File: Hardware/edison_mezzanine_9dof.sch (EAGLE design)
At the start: 43 parts, among them U1 LSM9DS0, U2 EDISON_CONNECTOR_FULLMOUNTING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, U3 EDISON_CONNECTOR_FULLHEADER

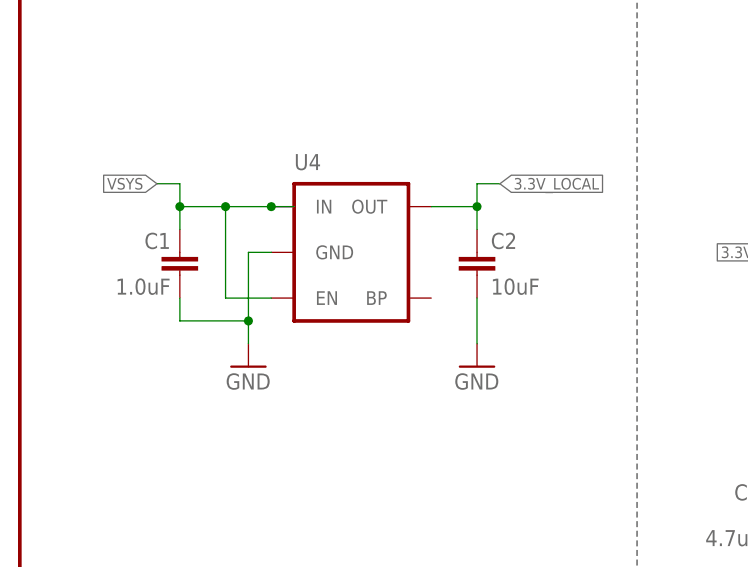
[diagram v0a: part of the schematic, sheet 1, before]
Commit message: Fixed hanging wire from LDO and added LDO chip name to schematic.
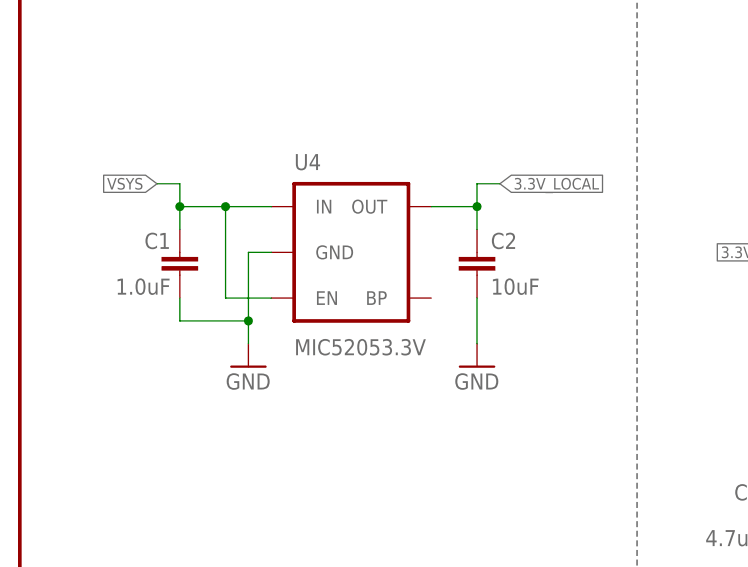
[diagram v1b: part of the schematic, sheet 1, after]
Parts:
- U4: value (none) -> MIC52053.3V
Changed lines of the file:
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@@
 <setting verticaltext="up"/>
 </settings>
-<grid distance="0.1" unitdist="inch" unit="inch" style="lines" multiple="1" display="yes" altdistance="0.01" altunitdist="inch" altunit="inch"/>
+<grid distance="0.1" unitdist="inch" unit="inch" style="lines" multiple="1" display="no" altdistance="0.01" altunitdist="inch" altunit="inch"/>
 <layers>
 <layer number="1" name="Top" color="4" fill="1" visible="no" active="no"/>
@@
 <part name="SJ2" library="SparkFun-Passives" deviceset="JUMPER-PAD-3-NC_BY_PASTE" device=""/>
 <part name="SJ1" library="SparkFun-Passives" deviceset="JUMPER-PAD-3-NC_BY_PASTE" device=""/>
-<part name="U4" library="SparkFun-PowerIC" deviceset="MIC5205" device="3.3V"/>
+<part name="U4" library="SparkFun-PowerIC" deviceset="MIC5205" device="3.3V" value="MIC52053.3V"/>
 <part name="C1" library="SparkFun-Capacitors" deviceset="1.0UF-16V-10%(0603)" device="" value="1.0uF"/>
 <part name="C4" library="SparkFun-Capacitors" deviceset="0.1UF-25V(+80/-20%)(0603)" device="" value="0.1uF"/>
@@
 <wire x1="27.94" y1="129.54" x2="22.86" y2="129.54" width="0.1524" layer="91"/>
 <wire x1="22.86" y1="129.54" x2="22.86" y2="139.7" width="0.1524" layer="91"/>
-<wire x1="30.48" y1="139.7" x2="27.94" y2="139.7" width="0.1524" layer="91"/>
-<wire x1="27.94" y1="139.7" x2="22.86" y2="139.7" width="0.1524" layer="91"/>
 <wire x1="22.86" y1="139.7" x2="17.78" y2="139.7" width="0.1524" layer="91"/>
-<junction x="22.86" y="139.7"/>
 <pinref part="C1" gate="G$1" pin="1"/>
 <wire x1="17.78" y1="139.7" x2="17.78" y2="137.16" width="0.1524" layer="91"/>
@@
 <label x="15.24" y="142.24" size="1.27" layer="95" rot="R180" xref="yes"/>
 <pinref part="U4" gate="G$1" pin="IN"/>
-<junction x="27.94" y="139.7"/>
-</segment>
-</net>
+<wire x1="22.86" y1="139.7" x2="27.94" y2="139.7" width="0.1524" layer="91"/>
+<junction x="22.86" y="139.7"/>
+</segment>
+</net>

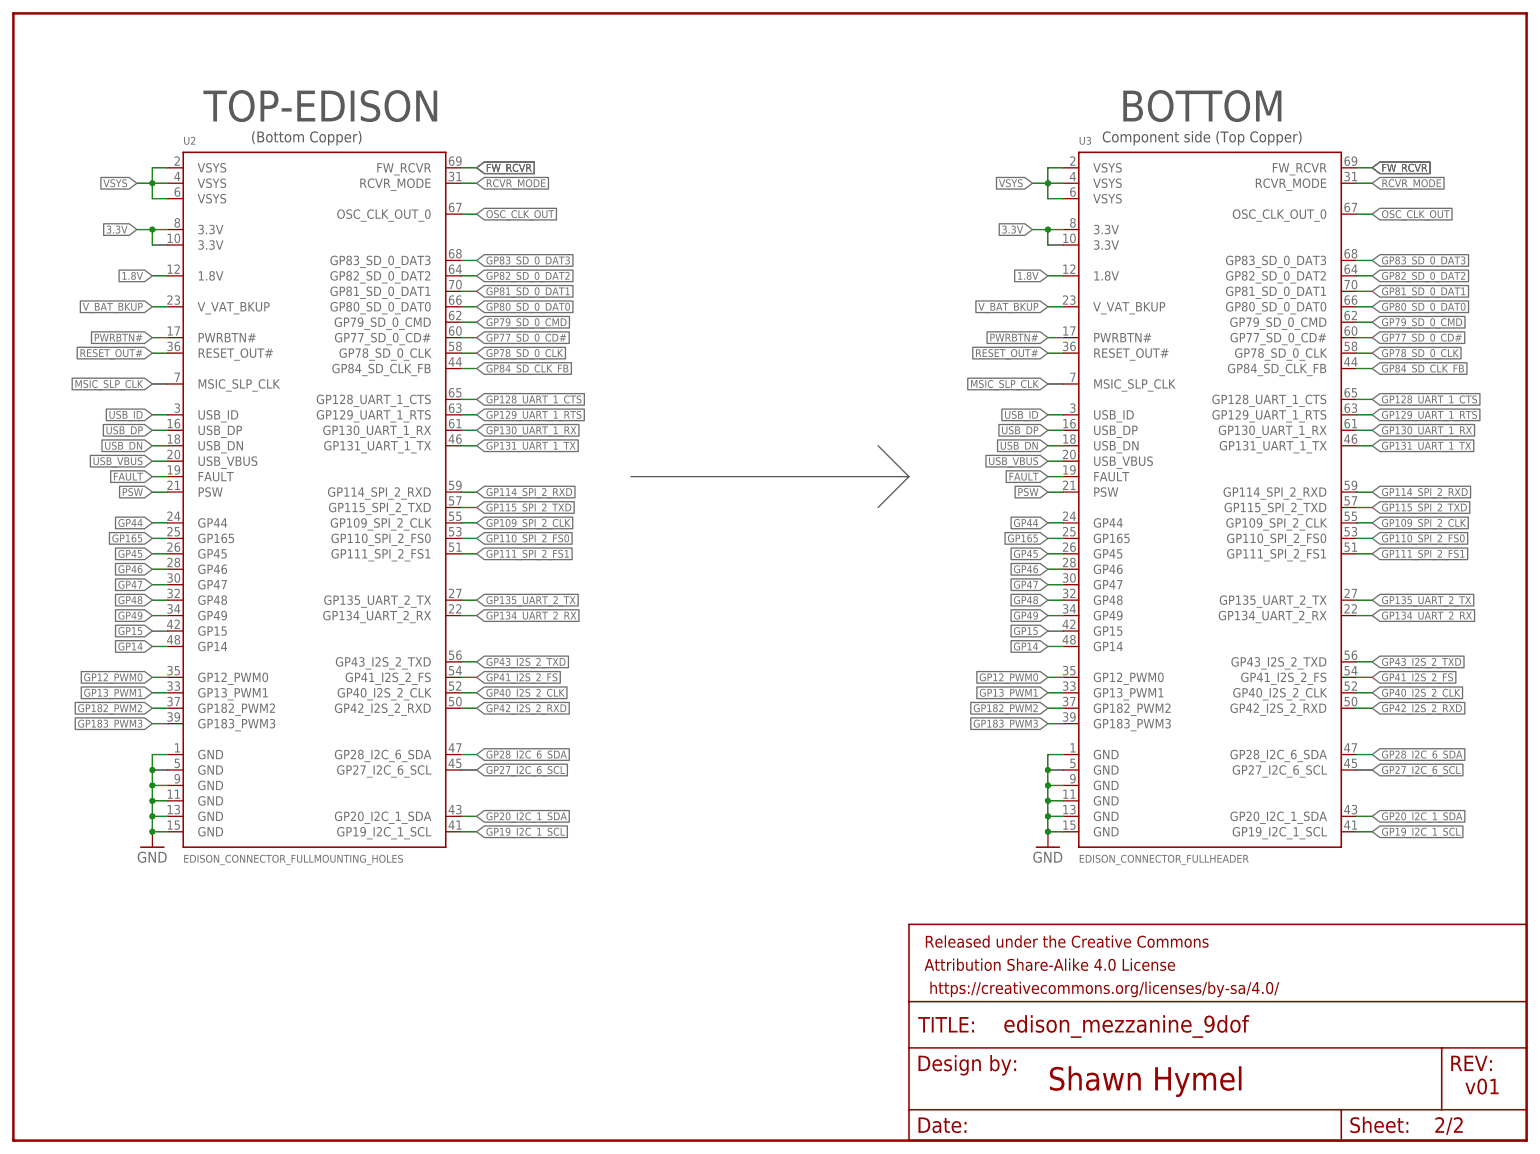
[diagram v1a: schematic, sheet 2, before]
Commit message: Added DCIN pin Corrected Header footprint Modified Name of board cleaned up units and added units cleaned up copper fills
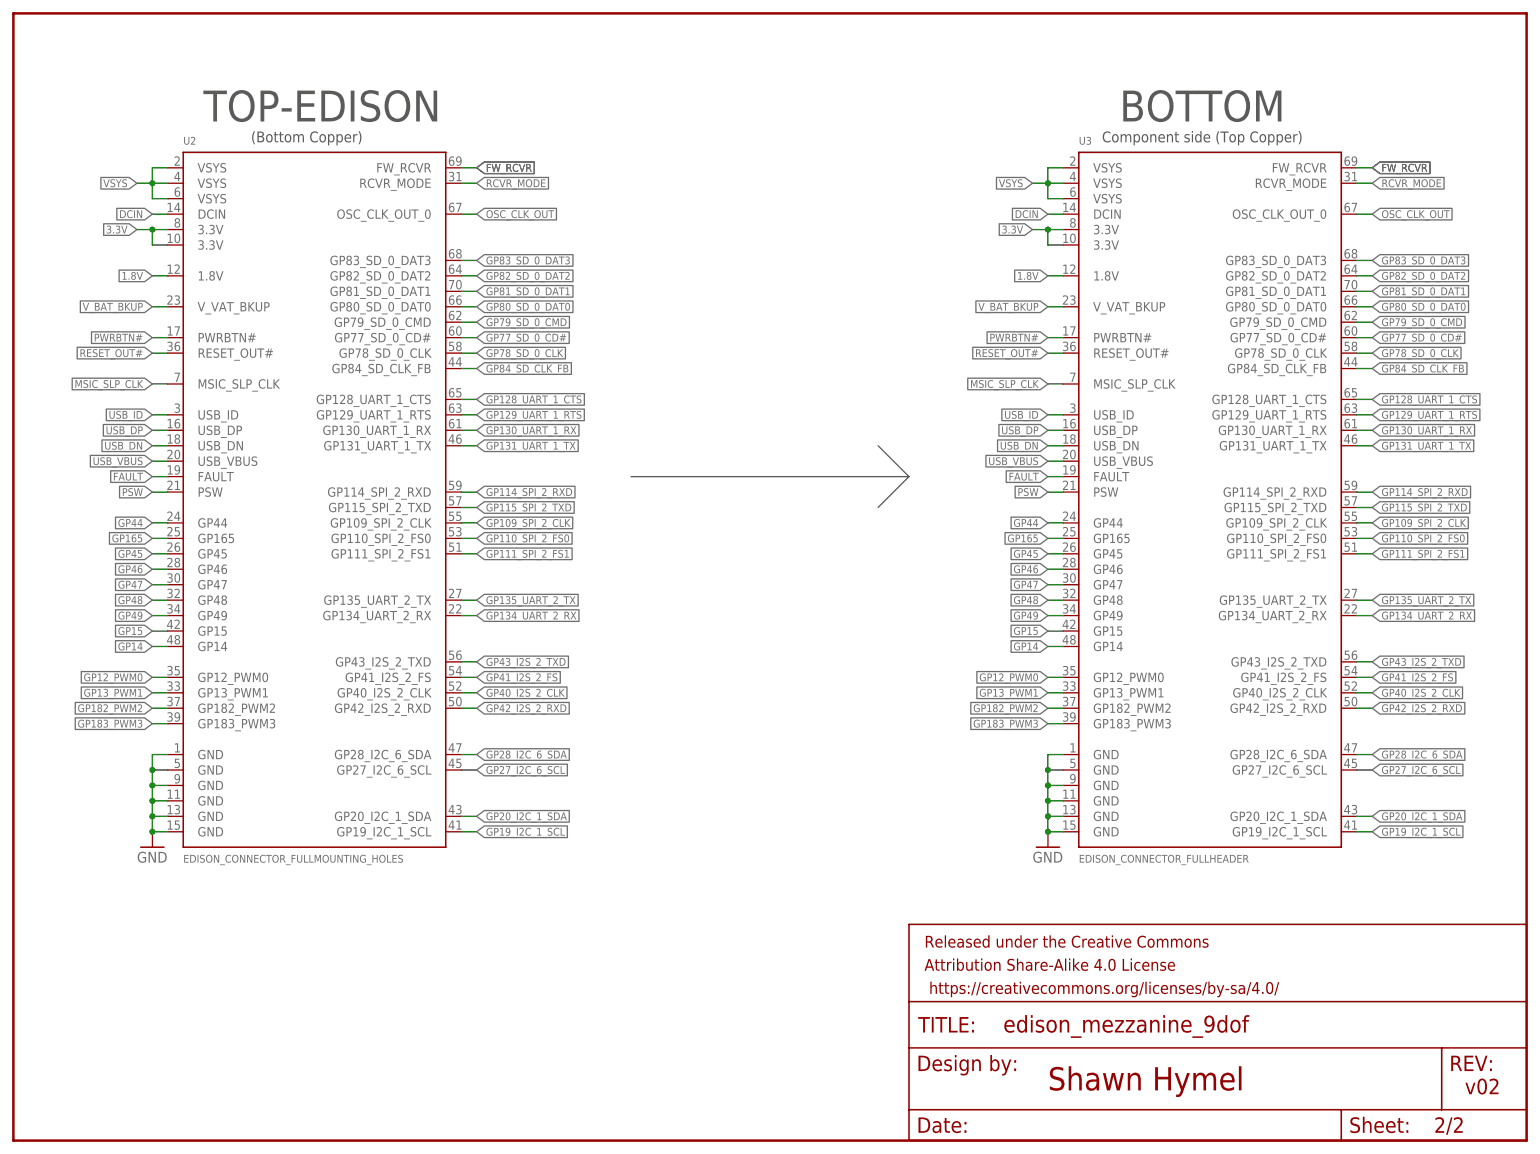
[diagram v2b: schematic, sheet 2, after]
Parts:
- removed FRAME3: FRAME-LETTER, SparkFun-Aesthetics:FRAME-LETTER
- R1, R2: value 4.7k -> DNP
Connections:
- new net DCIN: U2.DCIN, U3.DCIN
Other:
- note added: "v02"
- note removed: "v01"
- note removed: "v10"
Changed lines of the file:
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@@
 </classes>
 <parts>
-<part name="FRAME1" library="SparkFun-Aesthetics" deviceset="FRAME-LETTER" device=""/>
 <part name="LOGO2" library="SparkFun-Aesthetics" deviceset="OSHW-LOGO" device="S"/>
 <part name="LOGO3" library="SparkFun-Aesthetics" deviceset="SFE_LOGO_NAME_FLAME" device=".1_INCH"/>
@@
 <part name="C3" library="SparkFun-Capacitors" deviceset="1.0UF-16V-10%(0603)" device="" value="1.0uF"/>
 <part name="GND5" library="SparkFun-Aesthetics" deviceset="GND" device=""/>
-<part name="R1" library="SparkFun-Resistors" deviceset="10K-1%" device="RES-00824" value="4.7k"/>
-<part name="R2" library="SparkFun-Resistors" deviceset="10K-1%" device="RES-00824" value="4.7k"/>
+<part name="R1" library="SparkFun-Resistors" deviceset="10K-1%" device="RES-00824" value="DNP"/>
+<part name="R2" library="SparkFun-Resistors" deviceset="10K-1%" device="RES-00824" value="DNP"/>
 <part name="R3" library="SparkFun-Resistors" deviceset="10K-1%" device="RES-00824" value="10k"/>
 <part name="R4" library="SparkFun-Resistors" deviceset="10K-1%" device="RES-00824" value="10k"/>
@@
 <part name="FID1" library="SparkFun-Aesthetics" deviceset="FIDUCIAL" device="1X2"/>
 <part name="FID2" library="SparkFun-Aesthetics" deviceset="FIDUCIAL" device="1X2"/>
-<part name="FRAME2" library="SparkFun-Aesthetics" deviceset="FRAME-LETTER" device=""/>
-<part name="FRAME3" library="SparkFun-Aesthetics" deviceset="FRAME-LETTER" device=""/>
 <part name="SJ16" library="SparkFun-Passives" deviceset="JUMPER-PAD-2-NO" device="YES_SILK"/>
 <part name="SJ17" library="SparkFun-Passives" deviceset="JUMPER-PAD-2-NO" device="YES_SILK"/>
 <part name="FID3" library="SparkFun-Aesthetics" deviceset="FIDUCIAL" device="1X2"/>
 <part name="FID4" library="SparkFun-Aesthetics" deviceset="FIDUCIAL" device="1X2"/>
+<part name="FRAME1" library="SparkFun-Aesthetics" deviceset="FRAME-LETTER" device=""/>
+<part name="FRAME2" library="SparkFun-Aesthetics" deviceset="FRAME-LETTER" device=""/>
 </parts>
 <sheets>
@@
 <text x="45.72" y="25.4" size="2.54" layer="97" align="center">1</text>
 <text x="60.96" y="25.4" size="2.54" layer="97" align="center">0x6B</text>
-<text x="238.76" y="7.62" size="2.54" layer="94">v10</text>
-<text x="167.64" y="10.16" size="2.54" layer="94">Shawn Hymel</text>
+<text x="238.76" y="7.62" size="2.54" layer="94">v02</text>
+<text x="170.18" y="7.62" size="2.54" layer="94">Shawn Hymel</text>
 </plain>
 <instances>
-<instance part="FRAME1" gate="G$1" x="0" y="0"/>
-<instance part="FRAME1" gate="G$2" x="147.32" y="0"/>
 <instance part="LOGO2" gate="G$1" x="73.66" y="12.7"/>
 <instance part="LOGO3" gate="G$1" x="88.9" y="2.54"/>
@@
 <instance part="FID3" gate="G$1" x="246.38" y="30.48"/>
 <instance part="FID4" gate="G$1" x="241.3" y="30.48"/>
+<instance part="FRAME1" gate="G$1" x="0" y="0"/>
+<instance part="FRAME1" gate="G$2" x="147.32" y="0"/>
 </instances>
 <busses>
@@
 <text x="48.26" y="165.1" size="1.778" layer="92" align="center">(Bottom Copper)</text>
 <text x="170.18" y="10.16" size="3.81" layer="94" align="center-left">Shawn Hymel</text>
-<text x="238.76" y="7.62" size="2.54" layer="94">v01</text>
+<text x="238.76" y="7.62" size="2.54" layer="94">v02</text>
 </plain>
 <instances>
@@
 <instance part="GND4" gate="1" x="170.18" y="48.26"/>
 <instance part="FRAME2" gate="G$1" x="0" y="0"/>
-<instance part="FRAME3" gate="G$2" x="147.32" y="0"/>
+<instance part="FRAME2" gate="G$2" x="147.32" y="0"/>
 </instances>
 <busses>
@@
 </segment>
 </net>
+<net name="DCIN" class="0">
+<segment>
+<pinref part="U3" gate="G$1" pin="DCIN"/>
+<wire x1="172.72" y1="152.4" x2="170.18" y2="152.4" width="0.1524" layer="91"/>
+<label x="170.18" y="152.4" size="1.27" layer="95" rot="R180" xref="yes"/>
+</segment>
+<segment>
+<pinref part="U2" gate="G$1" pin="DCIN"/>
+<wire x1="25.4" y1="152.4" x2="22.86" y2="152.4" width="0.1524" layer="91"/>
+<label x="22.86" y="152.4" size="1.27" layer="95" rot="R180" xref="yes"/>
+</segment>
+</net>

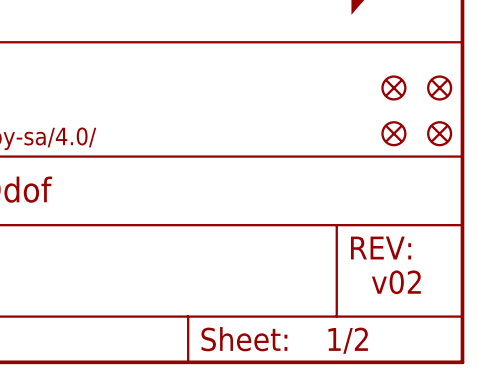
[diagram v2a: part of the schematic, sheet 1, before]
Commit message: Rev to 10, fix gnd and pwr, text
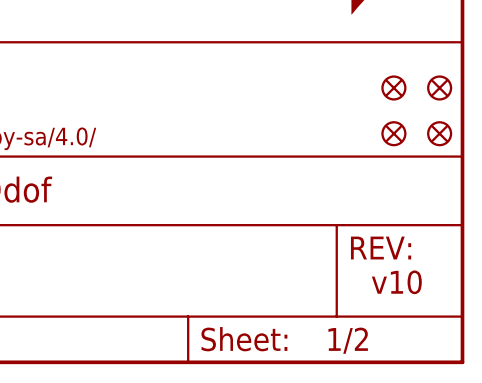
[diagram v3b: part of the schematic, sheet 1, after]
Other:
- note added: "v10"
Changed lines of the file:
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@@
 <?xml version="1.0" encoding="utf-8"?>
 <!DOCTYPE eagle SYSTEM "eagle.dtd">
-<eagle version="6.5.0">
+<eagle version="6.6.0">
 <drawing>
 <settings>
@@
 <layer number="254" name="cooling" color="7" fill="1" visible="yes" active="yes"/>
 </layers>
-<schematic xreflabel="%F%N/%S" xrefpart="1_/%S.%C%R">
+<schematic xreflabel="%F%N/%S" xrefpart="/%S.%C%R">
 <attributes>
 </attributes>
@@
 <text x="45.72" y="25.4" size="2.54" layer="97" align="center">1</text>
 <text x="60.96" y="25.4" size="2.54" layer="97" align="center">0x6B</text>
-<text x="238.76" y="7.62" size="2.54" layer="94">v02</text>
+<text x="238.76" y="7.62" size="2.54" layer="94">v10</text>
 <text x="170.18" y="7.62" size="2.54" layer="94">Shawn Hymel</text>
 </plain>
